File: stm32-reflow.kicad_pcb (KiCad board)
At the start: 4 copper layers, 64 x 59 mm, 62 parts, among them J1 TC2030, J10 63824-1, J11 63824-1, J12 63824-1, J2 Conn_01x04_Male, J3 Conn_01x03_Male, J4 Screw_Terminal_01x02, J5 Screw_Terminal_01x02, J6 Conn_02x08_Odd_Even, J7 63824-1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

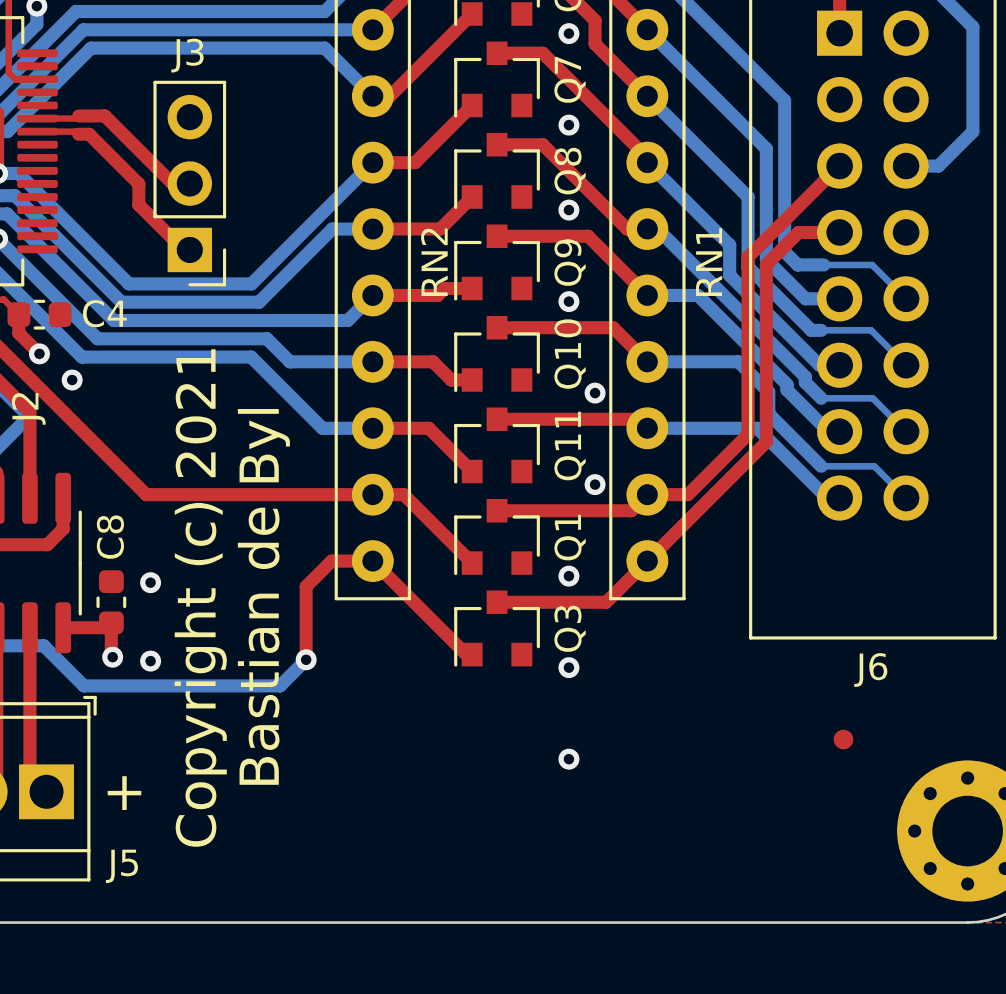
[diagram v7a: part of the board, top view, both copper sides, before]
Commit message: moved silkscreening around, added labels
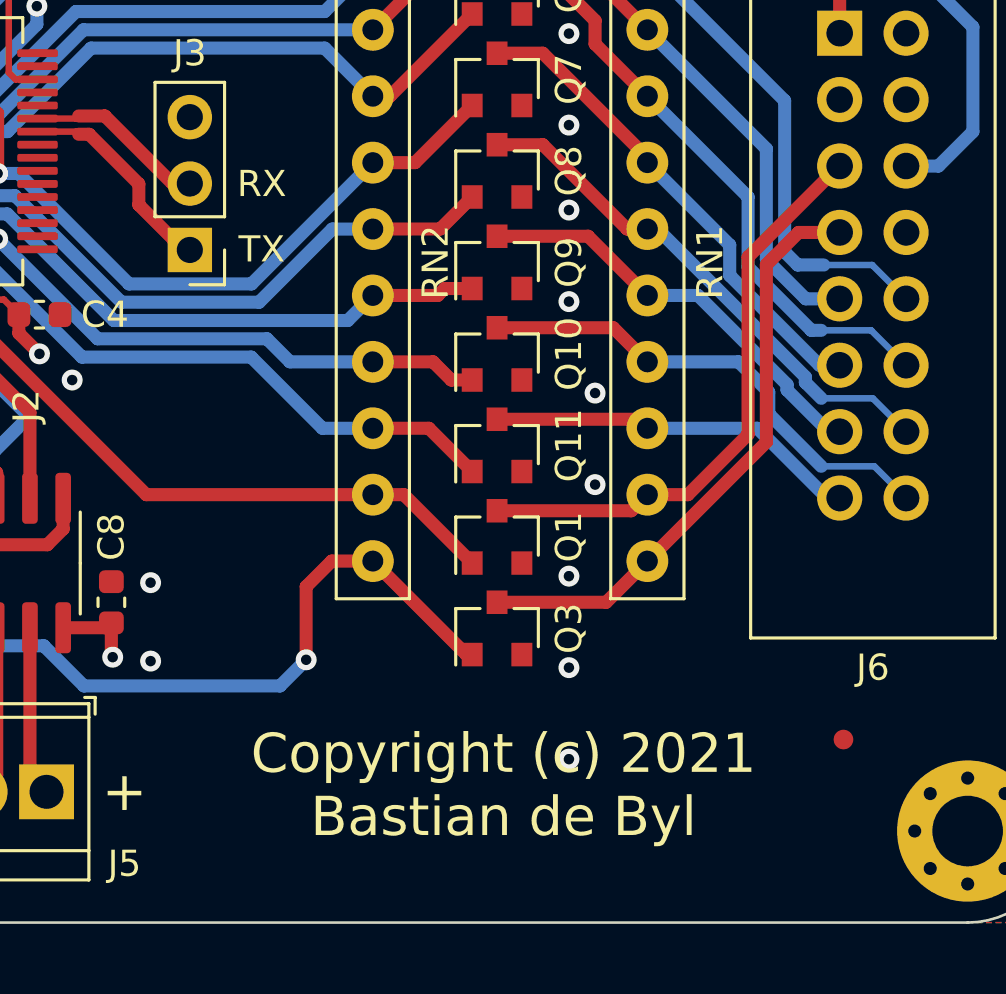
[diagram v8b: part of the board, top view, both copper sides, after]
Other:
- board text added: "DB0"
- board text added: "DB1"
- board text added: "DB2"
- board text added: "DB3"
- board text added: "DB4"
- board text added: "DB5"
- board text added: "DB6"
- board text added: "DB7"
- board text added: "LE"
- board text added: "LEDK"
- board text added: "MISO"
- board text added: "MOSI"
- board text added: "R/~{W}"
- board text added: "RS"
- board text added: "RX"
- board text added: "SCK"
- board text added: "TX"
- board text added: "VCC"
- board text added: "VEE"
- board text added: "VSS"
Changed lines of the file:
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@@
   (gr_line (start 175.5 77.75) (end 175.5 129.75) (layer "Edge.Cuts") (width 0.1))
   (gr_arc (start 172 74.25) (mid 174.474874 75.275126) (end 175.5 77.75) (layer "Edge.Cuts") (width 0.1))
-  (gr_text "LEDA" (at 172.8 99.2) (layer "B.SilkS")
-    (effects (font (size 1 1) (thickness 0.2)) (justify mirror))
+  (gr_text "R/~{W}" (at 170.85 106.75) (layer "B.SilkS")
+    (effects (font (size 1 1) (thickness 0.2)) (justify right mirror))
+  )
+  (gr_text "DB3" (at 166 112) (layer "B.SilkS")
+    (effects (font (size 1 1) (thickness 0.2)) (justify left mirror))
+  )
+  (gr_text "VSS" (at 170.85 101.75) (layer "B.SilkS")
+    (effects (font (size 1 1) (thickness 0.2)) (justify right mirror))
+  )
+  (gr_text "RS" (at 166 104.25) (layer "B.SilkS")
+    (effects (font (size 1 1) (thickness 0.2)) (justify left mirror))
+  )
+  (gr_text "DB5" (at 166 114.5) (layer "B.SilkS")
+    (effects (font (size 1 1) (thickness 0.2)) (justify left mirror))
+  )
+  (gr_text "VEE" (at 170.85 104.25) (layer "B.SilkS")
+    (effects (font (size 1 1) (thickness 0.2)) (justify right mirror))
+  )
+  (gr_text "LE" (at 166 106.8) (layer "B.SilkS")
+    (effects (font (size 1 1) (thickness 0.2)) (justify left mirror))
+  )
+  (gr_text "DB1" (at 166 109.5) (layer "B.SilkS")
+    (effects (font (size 1 1) (thickness 0.2)) (justify left mirror))
+  )
+  (gr_text "MISO" (at 128.25 110 90) (layer "B.SilkS")
+    (effects (font (size 1 1) (thickness 0.15)) (justify mirror))
+  )
+  (gr_text "DB0" (at 170.85 109.5) (layer "B.SilkS")
+    (effects (font (size 1 1) (thickness 0.2)) (justify right mirror))
+  )
+  (gr_text "VCC" (at 166 101.75) (layer "B.SilkS")
+    (effects (font (size 1 1) (thickness 0.2)) (justify left mirror))
+  )
+  (gr_text "DB2" (at 170.85 112) (layer "B.SilkS")
+    (effects (font (size 1 1) (thickness 0.2)) (justify right mirror))
+  )
+  (gr_text "MOSI" (at 130.75 110 90) (layer "B.SilkS")
+    (effects (font (size 1 1) (thickness 0.15)) (justify mirror))
+  )
+  (gr_text "DB6" (at 171.1 117) (layer "B.SilkS")
+    (effects (font (size 1 1) (thickness 0.2)) (justify right mirror))
+  )
+  (gr_text "DB7" (at 166 117) (layer "B.SilkS")
+    (effects (font (size 1 1) (thickness 0.2)) (justify left mirror))
+  )
+  (gr_text "SCK" (at 125.75 110.25 90) (layer "B.SilkS")
+    (effects (font (size 1 1) (thickness 0.15)) (justify mirror))
+  )
+  (gr_text "DB4" (at 170.85 114.5) (layer "B.SilkS")
+    (effects (font (size 1 1) (thickness 0.2)) (justify right mirror))
+  )
+  (gr_text "LEDA" (at 170.85 99.2) (layer "B.SilkS")
+    (effects (font (size 1 1) (thickness 0.2)) (justify right mirror))
+  )
+  (gr_text "LEDK" (at 166 99.25) (layer "B.SilkS")
+    (effects (font (size 1 1) (thickness 0.2)) (justify left mirror))
   )
   (gr_text "STM32 Reflow Board\nDesigned by Bastian de Byl" (at 154.25 108 90) (layer "B.SilkS")
     (effects (font (size 1.5 1.5) (thickness 0.3)) (justify mirror))
   )
+  (gr_text "RX" (at 145 105) (layer "F.SilkS")
+    (effects (font (size 1 1) (thickness 0.15)))
+  )
   (gr_text "+" (at 130.75 128.25) (layer "F.SilkS")
     (effects (font (size 1.5 1.5) (thickness 0.3)))
   )
-  (gr_text "Copyright (c) 2021\nBastian de Byl" (at 143.75 120.8 90) (layer "F.SilkS")
+  (gr_text "Copyright (c) 2021\nBastian de Byl" (at 154.25 128) (layer "F.SilkS")
     (effects (font (size 1.5 1.5) (thickness 0.3)))
   )
+  (gr_text "TX" (at 145 107.5) (layer "F.SilkS")
+    (effects (font (size 1 1) (thickness 0.15)))
+  )
   (gr_text "+" (at 139.750001 128.25) (layer "F.SilkS")
